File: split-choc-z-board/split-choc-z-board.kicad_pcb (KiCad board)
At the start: 2 copper layers, 147.1 x 106.5 mm, 79 parts, among them J1 USB4105-GF-A, J2 USB4105-GF-A, SW1 SW_SPST, SW10 SW_SPST, SW11 SW_SPST, SW12 SW_SPST, SW13 SW_SPST, SW14 SW_SPST, SW15 SW_SPST, SW16 SW_SPST, SW17 SW_SPST, SW18 SW_SPST, SW19 SW_SPST, SW2 SW_SPST, SW20 SW_SPST, SW21 SW_SPST, SW22 SW_SPST, SW3 SW_SPST, SW4 SW_SPST, SW5 SW_SPST, SW6 SW_SPST, SW7 SW_SPST, SW8 SW_SPST, SW9 SW_SPST, U2 RP2040, U3 NCP1117-3.3_SOT223, U4 W25Q128JVS, U5 USBLC6-2SC6, X1 ABM8-272-T3

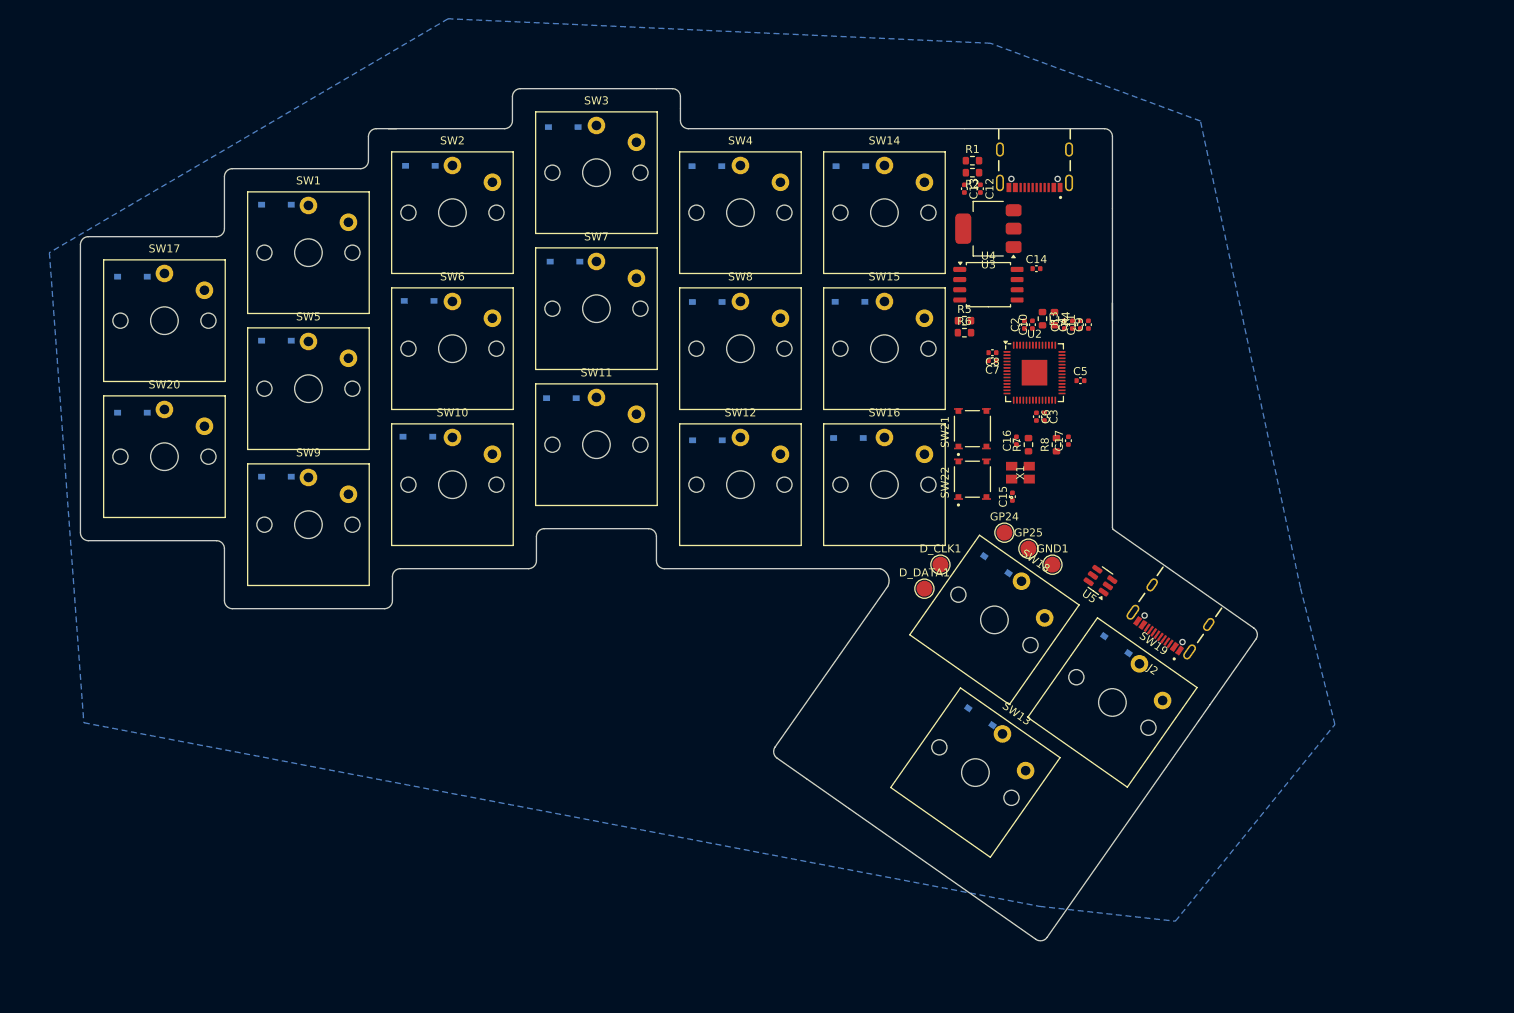
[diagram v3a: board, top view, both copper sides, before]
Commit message: Moved switch layout around and changed constraints for JLCPCB ⚡
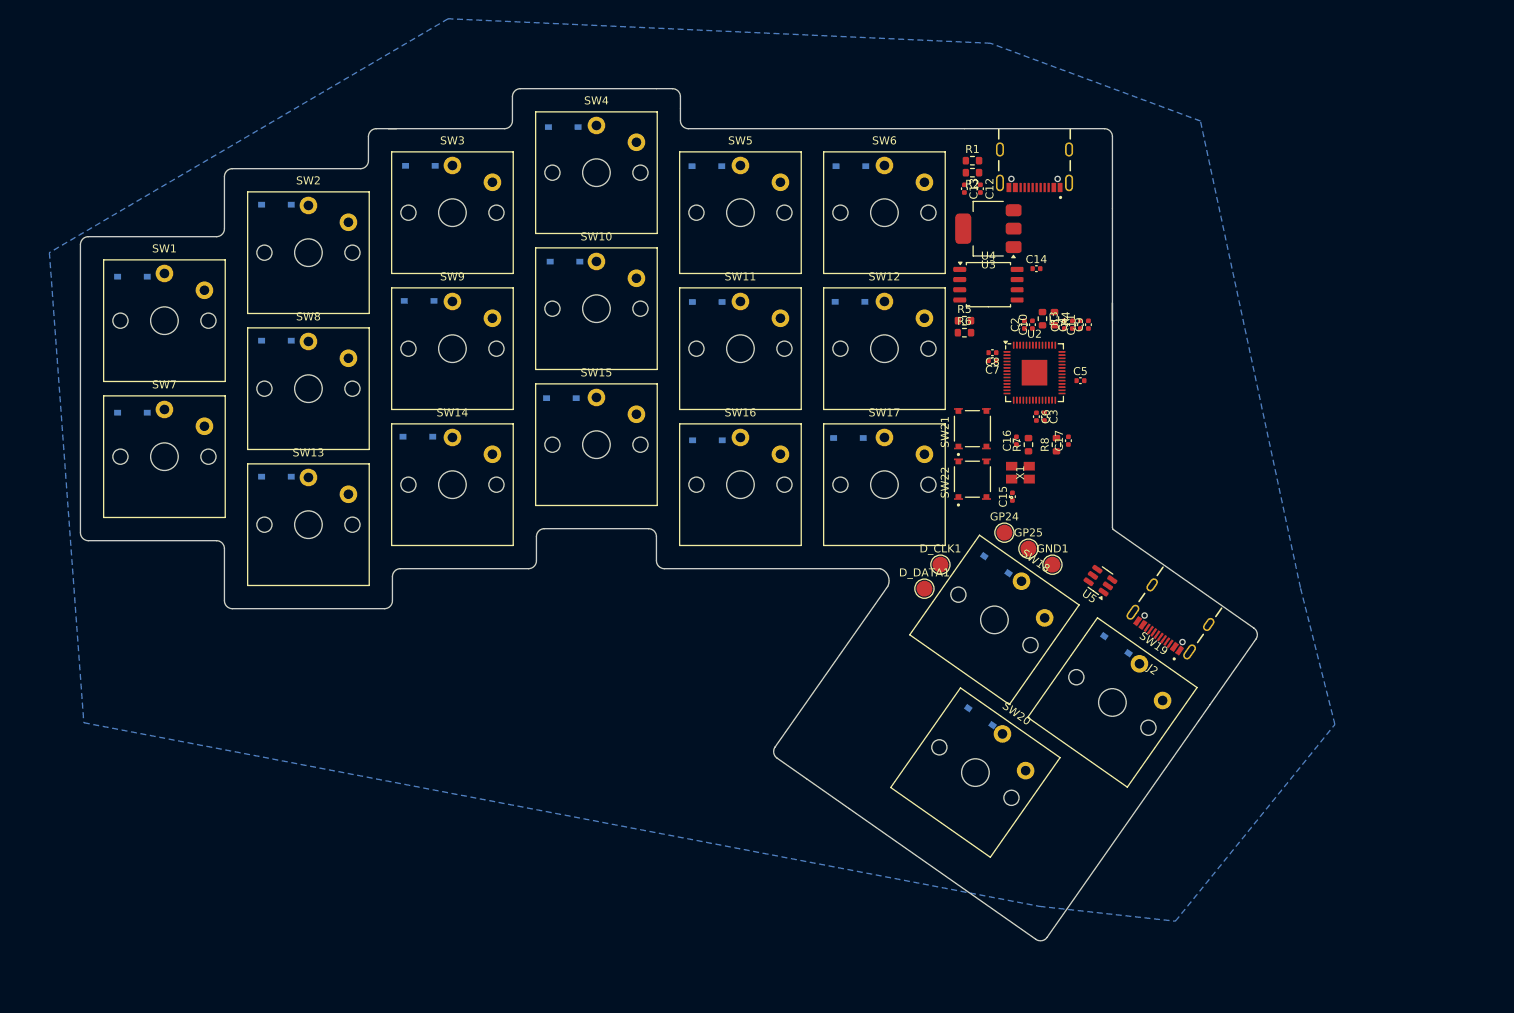
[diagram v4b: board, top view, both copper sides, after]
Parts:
- moved SW20 108.8 mm to (137.4, 126.0), turned to -35 degrees
- moved SW17 92.3 mm to (126.0, 90.0)
- moved SW13 88.9 mm to (54.0, 95.0), turned to 0 degrees
- moved SW14 63.8 mm to (72.0, 90.0)
- moved SW5 58.3 mm to (108.0, 56.0)
- moved SW7 57.1 mm to (36.0, 86.5)
- moved SW6 56.6 mm to (126.0, 56.0)
- moved SW8 54.2 mm to (54.0, 78.0)
- moved SW15 37.9 mm to (90.0, 85.0)
- moved SW10 28.4 mm to (90.0, 68.0)
- moved SW9 28.4 mm to (72.0, 73.0)
- moved SW12 24.8 mm to (126.0, 73.0)
- moved SW11 21.6 mm to (108.0, 73.0)
- moved SW1 19.9 mm to (36.0, 69.5)
- moved SW2 18.7 mm to (54.0, 61.0)
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
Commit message: Finalized component placement! 💡
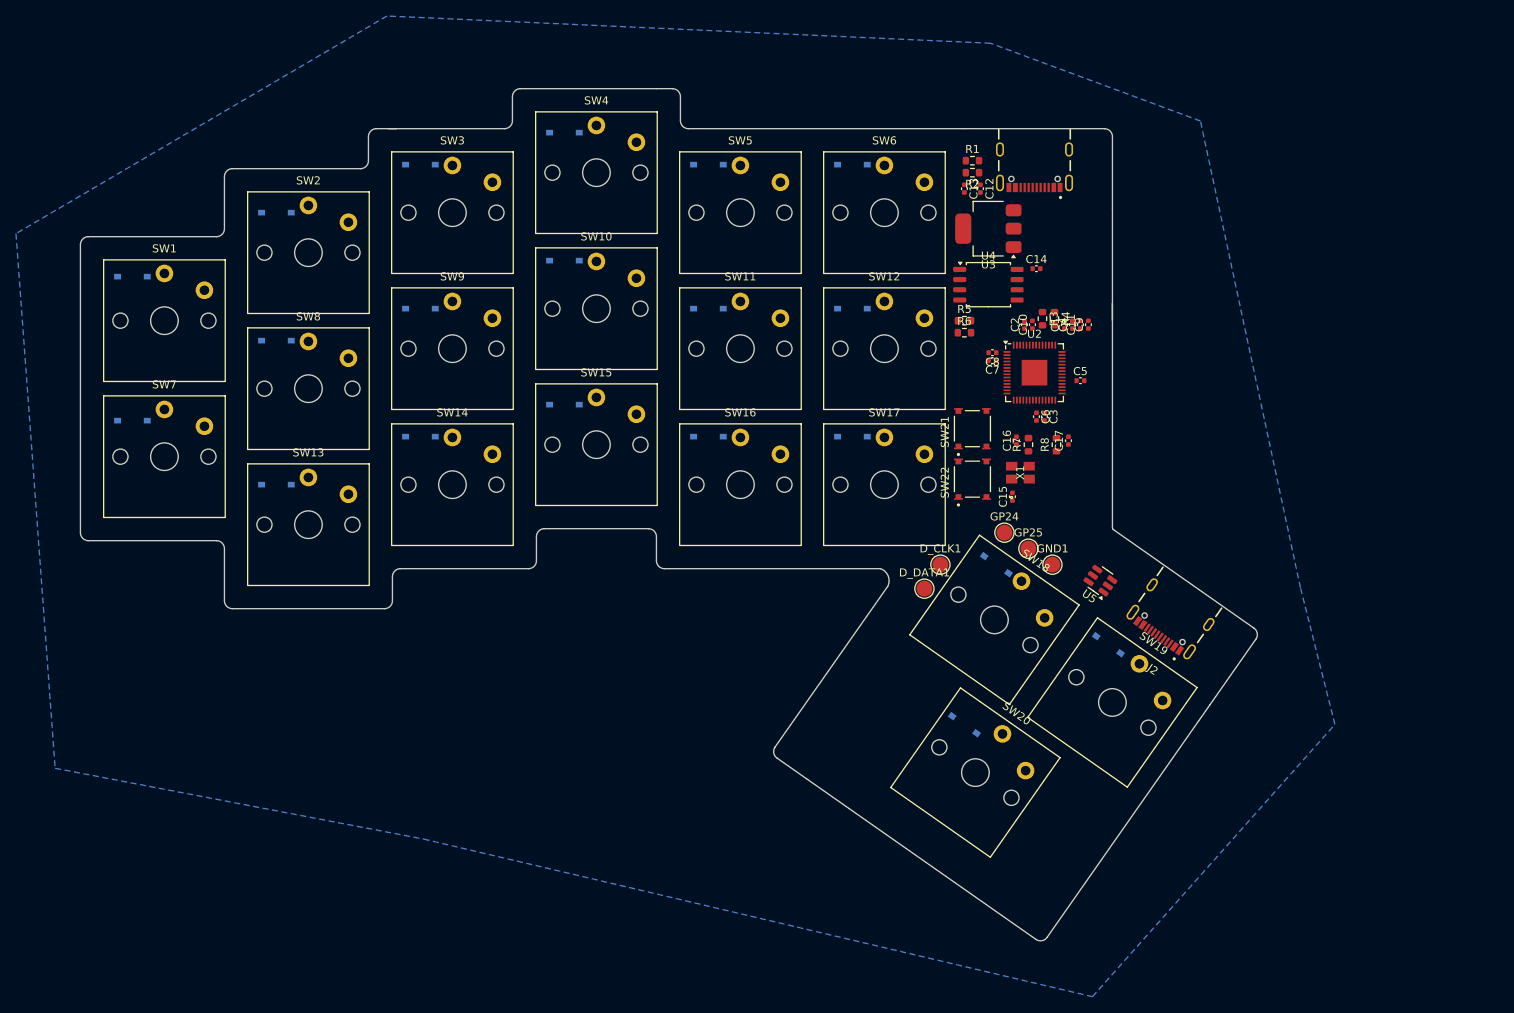
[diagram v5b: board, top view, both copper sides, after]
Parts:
- moved D20 111.1 mm to (136.0, 120.0), turned to -35 degrees
- moved D13 92.7 mm to (50.0, 90.0), turned to 0 degrees
- moved D17 92.2 mm to (122.0, 84.0)
- moved D14 63.6 mm to (68.0, 84.0)
- moved D5 58.3 mm to (104.0, 50.0)
- moved D7 57.6 mm to (32.0, 82.0)
- moved D6 56.8 mm to (122.0, 50.0)
- moved D8 54.1 mm to (50.0, 72.0)
- moved D15 37.9 mm to (86.0, 80.0)
- moved D10 28.6 mm to (86.0, 62.0)
- moved D9 27.7 mm to (68.0, 68.0)
- moved D12 24.5 mm to (122.0, 68.0)
- moved D11 21.5 mm to (104.0, 68.0)
- moved D1 20.1 mm to (32.0, 64.0)
- moved D2 18.9 mm to (50.0, 56.0)
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
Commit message: Almost done routing left side
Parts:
- moved C9 3.53 mm to (150.4, 73.3), turned to 0 degrees
- moved C11 2.35 mm to (150.4, 72.3), turned to 0 degrees
- moved C1 1.93 mm to (150.4, 70.3), turned to 0 degrees
- moved C4 1.62 mm to (150.4, 71.3), turned to 0 degrees
- moved C2 0.85 mm to (144.3, 70.0)
- moved C10 0.75 mm to (145.2, 70.0)
- moved R3 0.70 mm to (146.4, 69.2)
- moved R4 0.70 mm to (147.9, 69.2)
- moved C7 0.55 mm to (139.6, 74.0)
- moved C8 0.55 mm to (139.6, 73.0)
- moved R1 0.10 mm to (137.0, 49.6)
- moved R2 0.10 mm to (137.0, 51.1)
- turned R7 to -90 degrees
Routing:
- net /Col_3: track 0.00 -> 242.5 mm, vias 0 -> 2
- net /Col_4: track 0.00 -> 189.6 mm, vias 0 -> 1
- net /Col_2: track 0.00 -> 176.9 mm, vias 0 -> 1
- net /Col_1: track 0.00 -> 156.4 mm
- net /Row_2: track 0.00 -> 151.1 mm, vias 0 -> 1
- net /Row_1: track 0.00 -> 149.2 mm, vias 0 -> 1
- net VBUS: track 0.00 -> 111.0 mm, vias 0 -> 4
- net /Row_4: track 0.00 -> 104.9 mm, vias 0 -> 1
- net /Row_3: track 0.00 -> 90.0 mm, vias 0 -> 1
- net /Row_5: track 0.00 -> 62.7 mm
- net /B-B_D+: track 0.00 -> 48.9 mm, vias 0 -> 2
- net /B-B_D-: track 0.00 -> 47.8 mm
- net +3V3: track 0.00 -> 43.8 mm
- net /DEBUG_DATA: track 0.00 -> 34.8 mm, vias 0 -> 2
- net /DEBUG_CLK: track 0.00 -> 27.9 mm, vias 0 -> 2
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
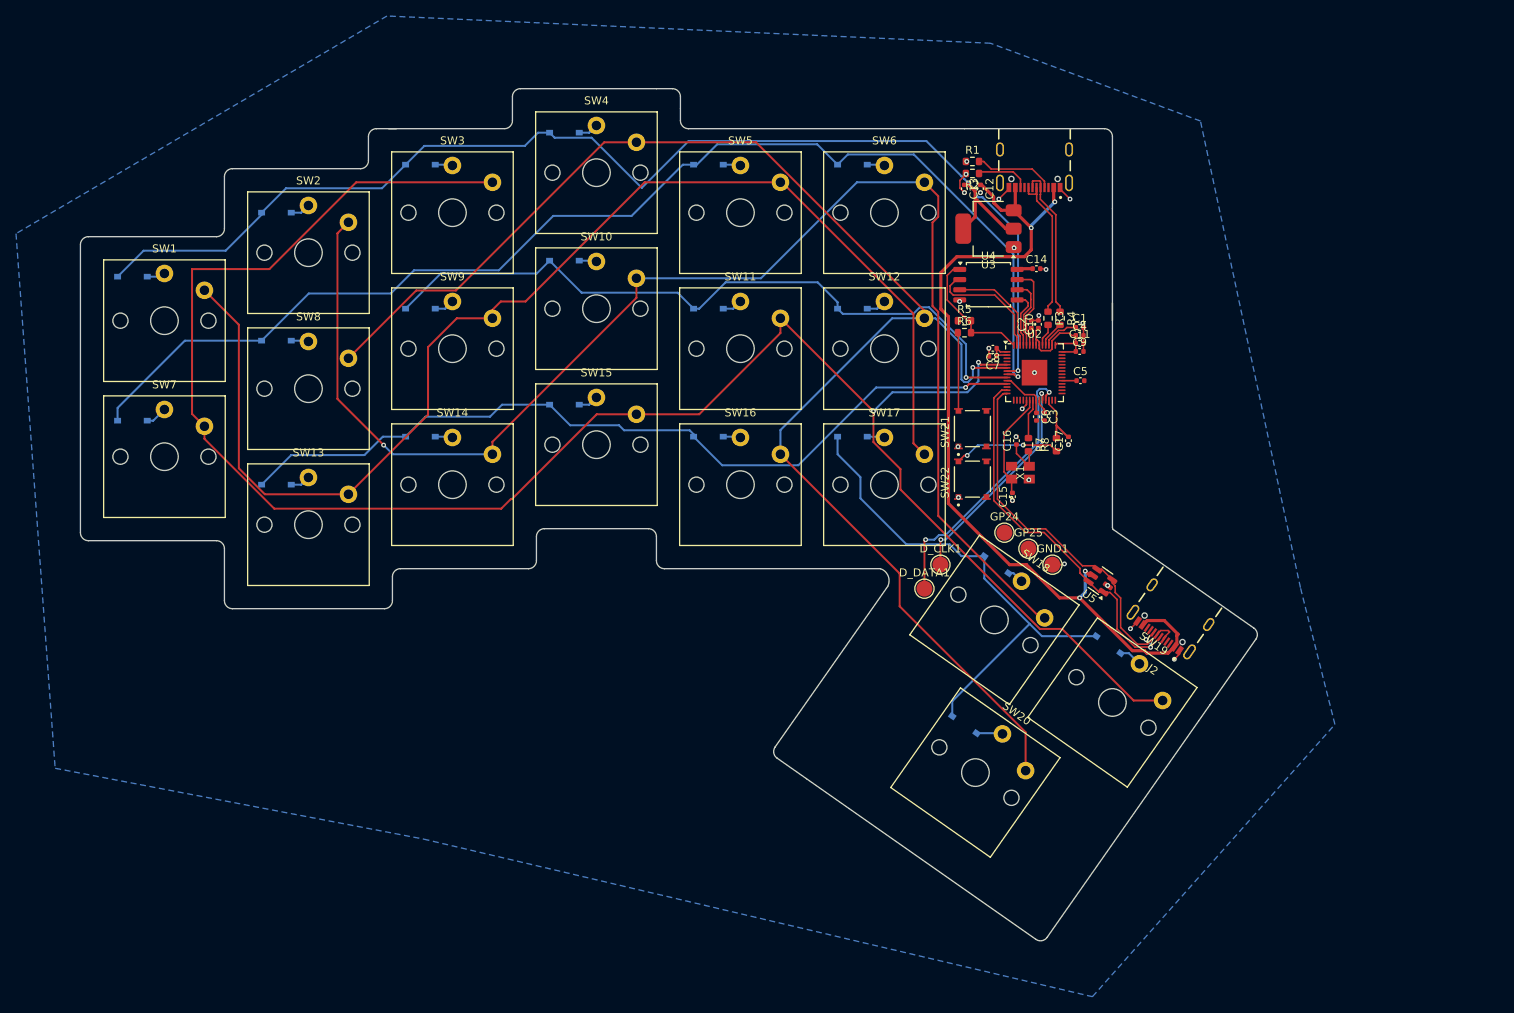
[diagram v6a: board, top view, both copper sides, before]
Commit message: Almost finished left half routing
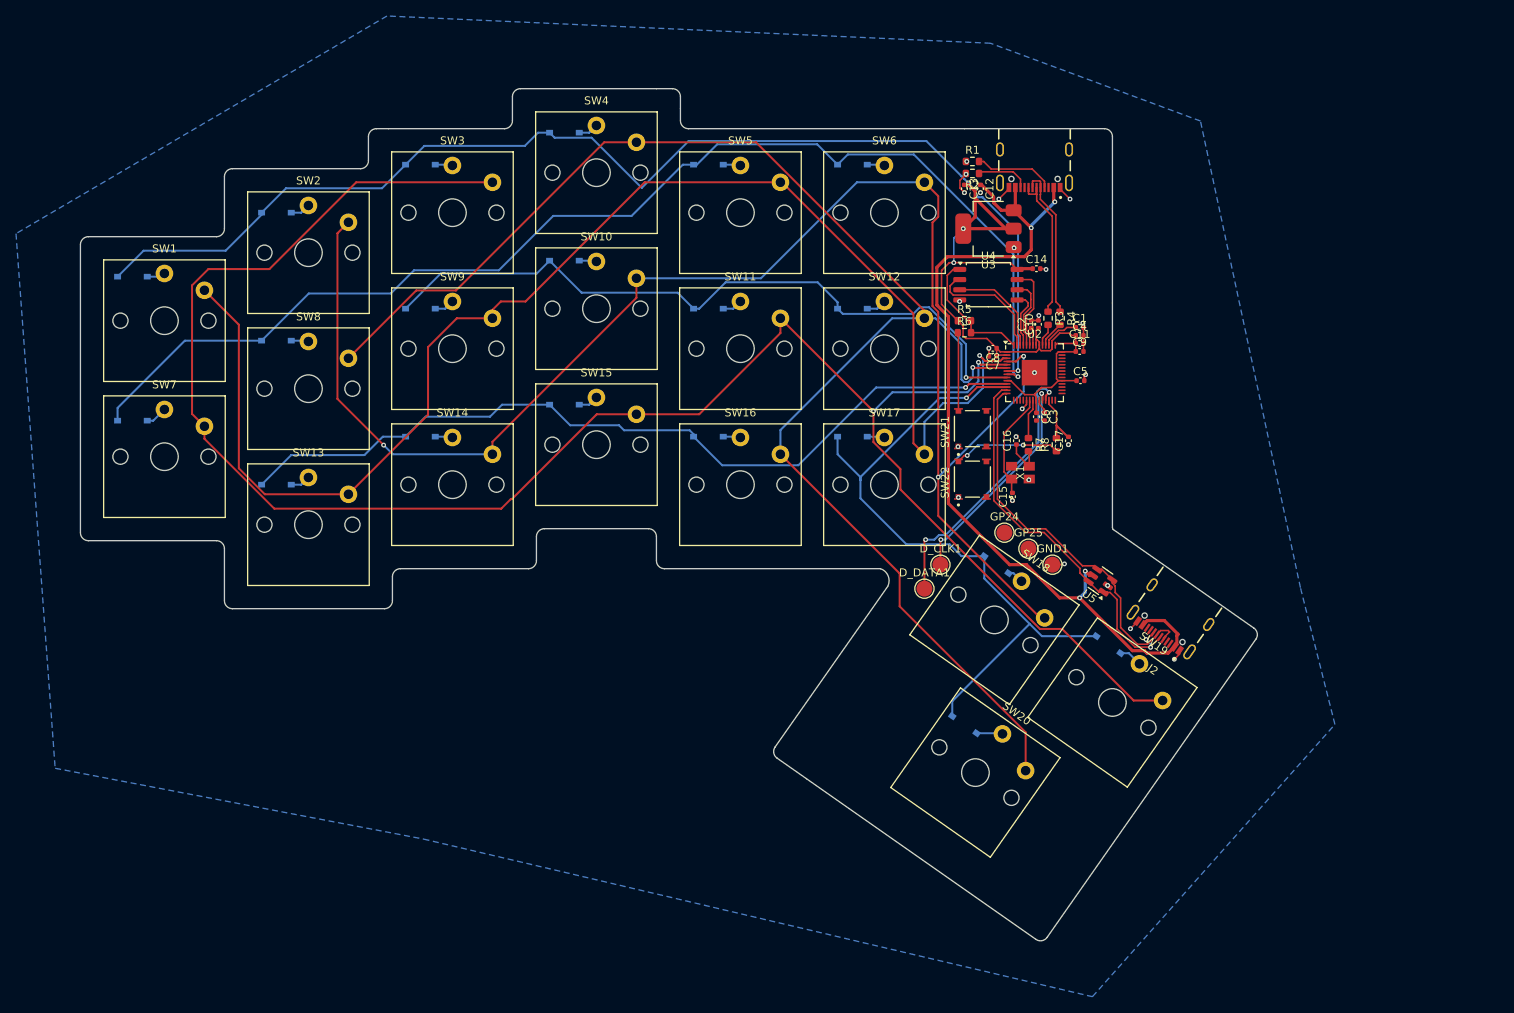
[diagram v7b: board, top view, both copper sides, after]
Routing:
- net +3V3: track 43.8 -> 91.9 mm, vias 0 -> 2
- net /Row_5: track 62.7 -> 86.1 mm, vias 0 -> 1
- net /Col_2: track 176.9 -> 198.8 mm, vias 1 -> 3
- net /Col_1: track 156.4 -> 177.6 mm, vias 0 -> 1
- net /Col_3: track 242.5 -> 241.3 mm
- net VBUS: track 111.0 -> 112.1 mm
- net GND: track 20.4 -> 21.2 mm, vias 24 -> 25
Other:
- outline, holes or cut-outs redrawn

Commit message: Routed left side
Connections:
- J1 pad SH1: GND -> unconnected-(J1-SHELL_GND-PadSH1)
- J1 pad SH2: GND -> unconnected-(J1-SHELL_GND__1-PadSH2)
- J1 pad SH3: GND -> unconnected-(J1-SHELL_GND__2-PadSH3)
- J2 pad SH1: GND -> unconnected-(J2-SHELL_GND-PadSH1)
- J2 pad SH2: GND -> unconnected-(J2-SHELL_GND__1-PadSH2)
- J2 pad SH3: GND -> unconnected-(J2-SHELL_GND__2-PadSH3)
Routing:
- net /GP25: track 0.00 -> 30.0 mm, vias 0 -> 2
- net /GP24: track 0.00 -> 29.0 mm, vias 0 -> 2
- net GND: track 21.2 -> 44.5 mm, vias 25 -> 28
- net +1V1: track 8.72 -> 26.4 mm, vias 0 -> 3
